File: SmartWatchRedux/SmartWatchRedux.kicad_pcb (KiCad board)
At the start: 2 copper layers, 20.3 x 65.1 mm, 6 parts, among them CN1 27C256Socket, U1 ROM, U2 DS1315, Y1 32.768 KHz

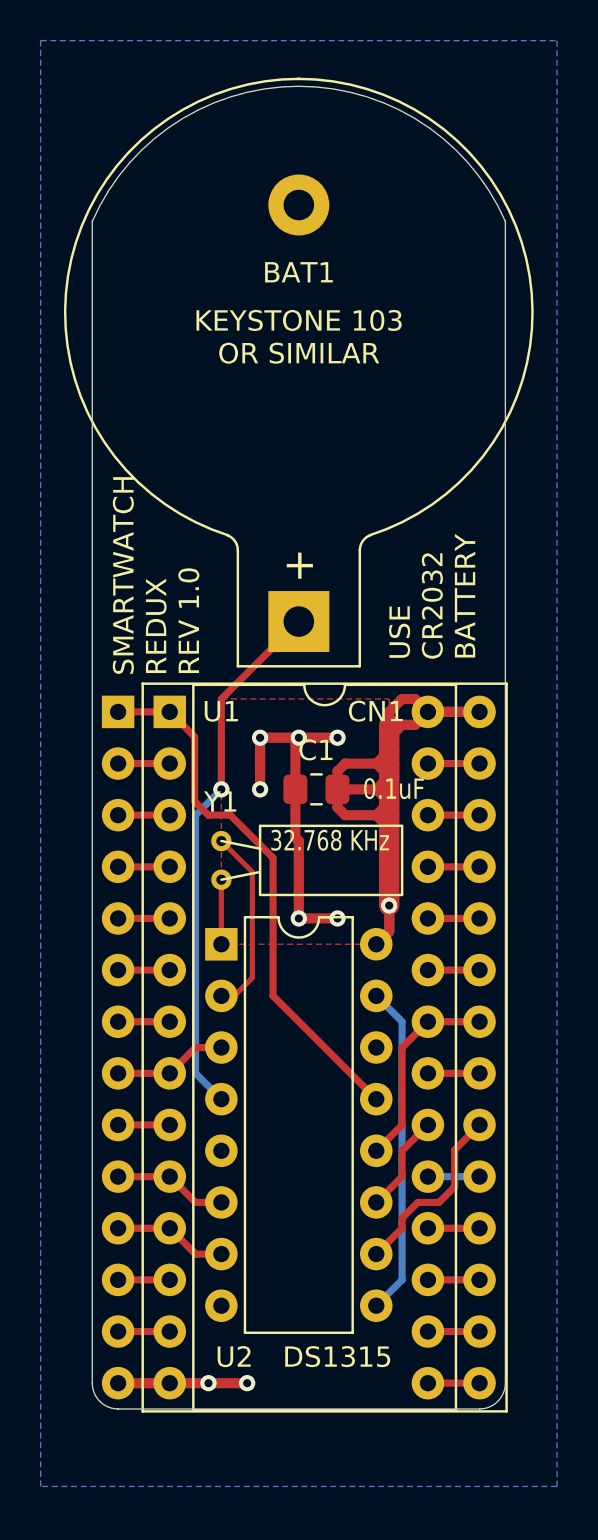
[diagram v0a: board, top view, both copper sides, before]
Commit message: Additional silkscreen text and refinements.
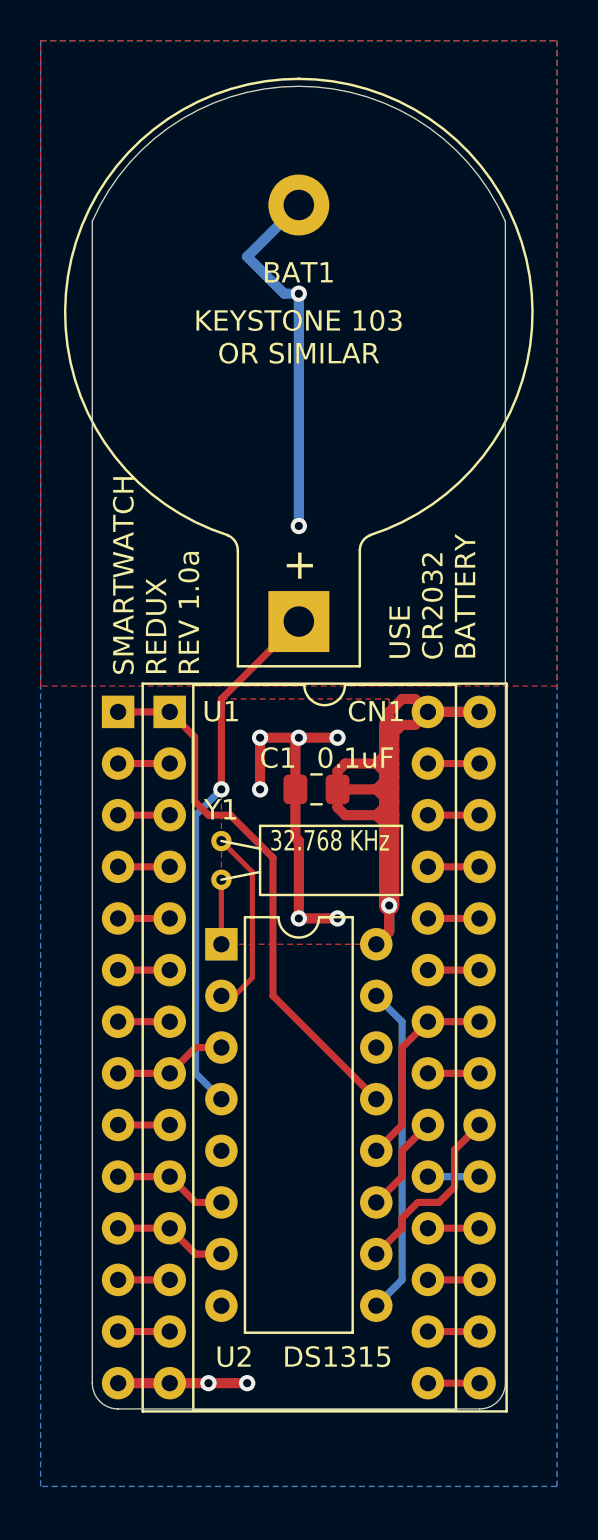
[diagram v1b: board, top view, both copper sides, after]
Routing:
- net GND: track 23.6 -> 42.0 mm, vias 8 -> 10
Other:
- board text added: "Circuit is the reference design from the DS1315 datasheet and confirmed to match a real DS1216-E SmartWatch. Board layout by Jayeson Lee-Steere and placed into the public domain."
- board text added: "SMARTWATCH REDUX REV 1.0a"
- board text removed: "SMARTWATCH REDUX REV 1.0"

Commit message: Refinements to SmartWatchRedux and ATD-20-Redux after assembling initial run of boards.
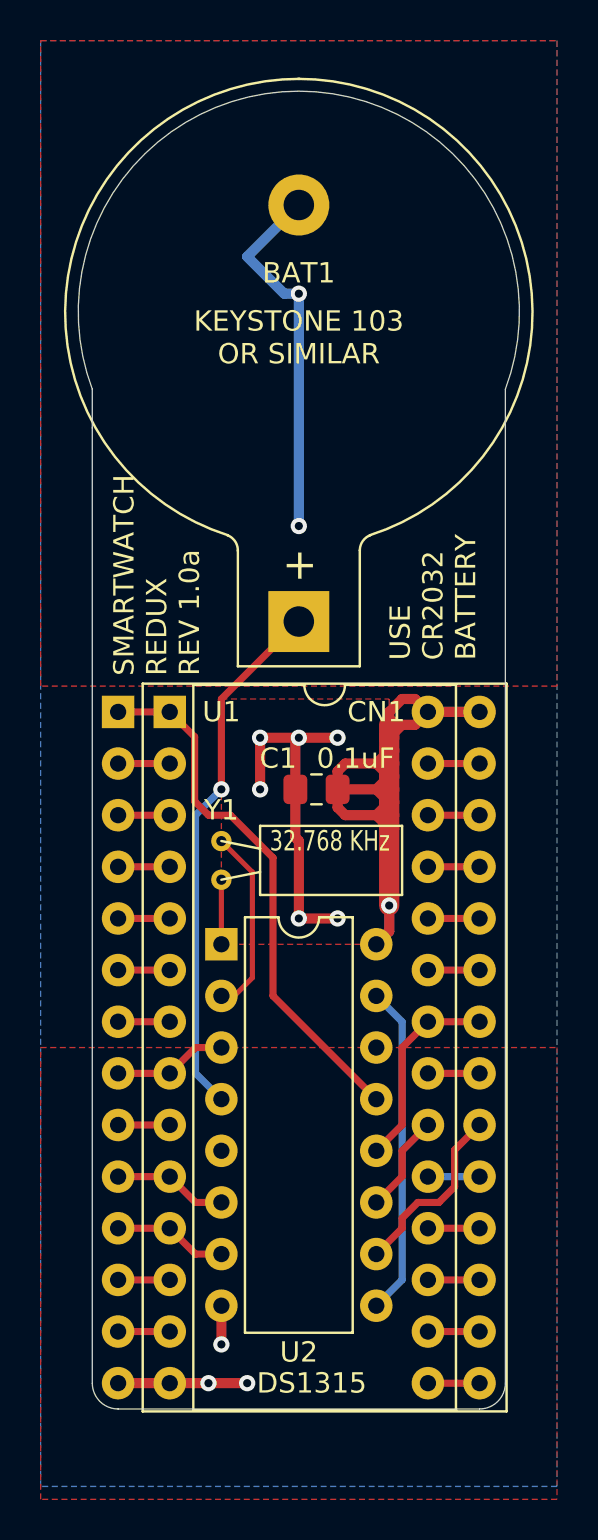
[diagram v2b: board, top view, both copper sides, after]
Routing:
- net GND: track 42.0 -> 43.9 mm, vias 10 -> 11
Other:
- board size 20.3 x 65.1 mm -> 21.7 x 64.8 mm
- board text added: "CUT FLUSH BEFORE SOLDERING"
- board text added: "https://github.com/ JayesonLS/TandyCircuitsAndLogic/ tree/master/SmartWatchRedux"
